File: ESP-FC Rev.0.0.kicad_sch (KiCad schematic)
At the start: 0 parts

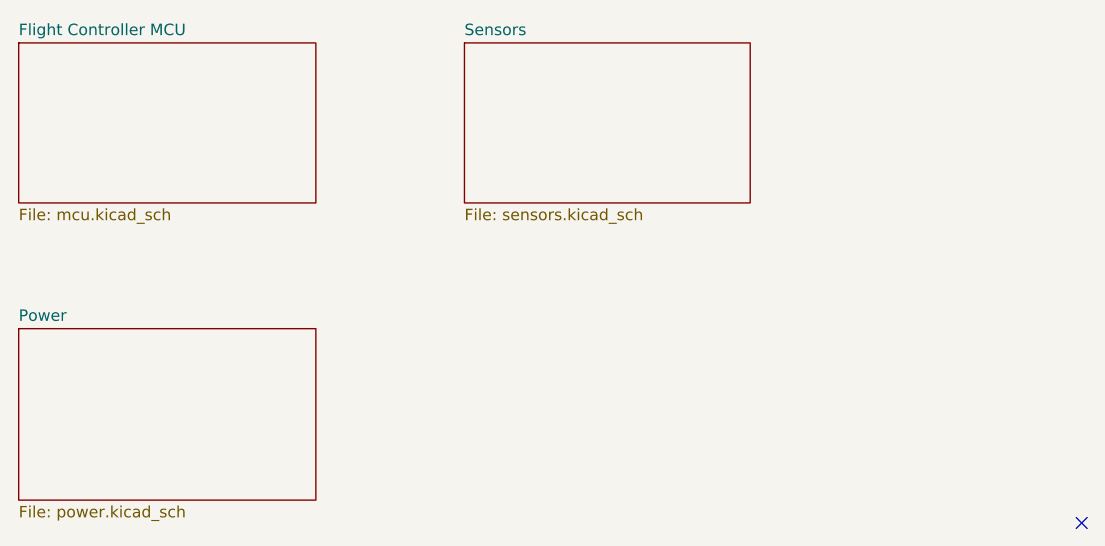
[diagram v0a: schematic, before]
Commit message: power sch. done, MCU powering as well
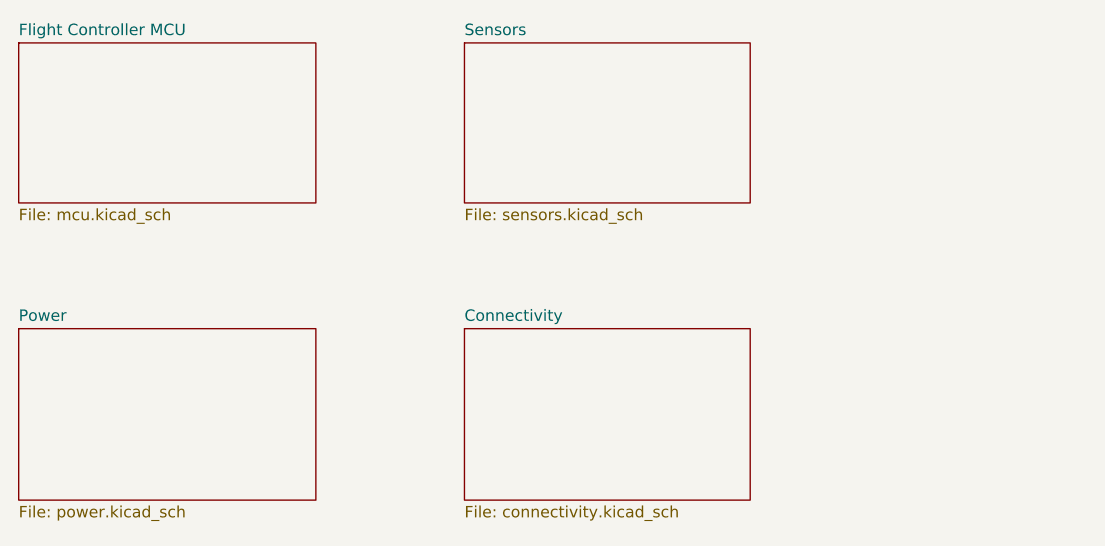
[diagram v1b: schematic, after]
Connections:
- no-connect marks 1 -> 0
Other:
- added sheet Connectivity (connectivity.kicad_sch)
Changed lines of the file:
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@@
 	(generator_version "10.0")
 	(paper "A4")
-	(no_connect
-		(at 143.51 82.55)
+	(sheet
+		(at 74.93 60.96)
+		(size 31.75 19.05)
+		(exclude_from_sim no)
+		(in_bom yes)
+		(on_board yes)
+		(dnp no)
+		(fields_autoplaced yes)
+		(stroke
+			(width 0.1524)
+			(type solid)
+		)
+		(fill
+			(color 0 0 0 0)
+		)
+		(property "Sheetname" "Connectivity"
+			(at 74.93 60.2484 0)
+			(show_name no)
+			(do_not_autoplace no)
+			(effects
+				(font
+					(size 1.27 1.27)
+				)
+				(justify left bottom)
+			)
+		)
+		(property "Sheetfile" "connectivity.kicad_sch"
+			(at 74.93 80.5946 0)
+			(show_name no)
+			(do_not_autoplace no)
+			(effects
+				(font
+					(size 1.27 1.27)
+				)
+				(justify left top)
+			)
+		)
+		(instances
+			(project "ESP-FC Rev.0.0"
+				(path "/3e1204b2-b79a-4f53-9cc5-58f8ed54619c"
+					(page "5")
+				)
+			)
+		)
 	)
 	(sheet

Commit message: Small ammendments
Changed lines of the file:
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@@
 		(on_board yes)
 		(dnp no)
-		(fields_autoplaced yes)
 		(stroke
 			(width 0.1524)
@@
 				)
 				(justify left top)
+			)
+		)
+		(property "Sheettext" "CONN."
+			(at 90.932 70.358 0)
+			(show_name no)
+			(do_not_autoplace no)
+			(effects
+				(font
+					(size 2.54 2.54)
+					(bold yes)
+				)
 			)
 		)
@@
 	(sheet
 		(at 25.4 29.21)
-		(size 33.02 17.78)
+		(size 31.75 17.78)
 		(exclude_from_sim no)
 		(in_bom yes)
 		(on_board yes)
 		(dnp no)
-		(fields_autoplaced yes)
 		(stroke
 			(width 0.1524)
@@
 				)
 				(justify left top)
+			)
+		)
+		(property "Sheettext" "MCU"
+			(at 41.402 37.338 0)
+			(show_name no)
+			(do_not_autoplace no)
+			(effects
+				(font
+					(size 2.54 2.54)
+					(bold yes)
+				)
 			)
 		)
@@
 		(on_board yes)
 		(dnp no)
-		(fields_autoplaced yes)
 		(stroke
 			(width 0.1524)
@@
 				)
 				(justify left top)
+			)
+		)
+		(property "Sheettext" "SENSORS"
+			(at 91.44 37.846 0)
+			(show_name no)
+			(do_not_autoplace no)
+			(effects
+				(font
+					(size 2.54 2.54)
+					(bold yes)
+				)
 			)
 		)
@@
 	(sheet
 		(at 25.4 60.96)
-		(size 33.02 19.05)
+		(size 31.75 19.05)
 		(exclude_from_sim no)
 		(in_bom yes)
 		(on_board yes)
 		(dnp no)
-		(fields_autoplaced yes)
 		(stroke
 			(width 0.1524)
@@
 			)
 		)
+		(property "Sheettext" "POWER"
+			(at 41.402 70.104 0)
+			(show_name no)
+			(do_not_autoplace no)
+			(effects
+				(font
+					(size 2.54 2.54)
+					(bold yes)
+				)
+			)
+		)
